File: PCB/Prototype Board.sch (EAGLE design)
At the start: 65 parts, among them J1 USB Type C, J3 Connector, J4 Battery Connector, Q1 S8050, Q10 20V/0.2A/8MHz/1.2Ω/1Vth, Q12 20V/0.2A/8MHz/1.2Ω/1Vth, Q14 20V/0.2A/8MHz/1.2Ω/1Vth, Q16 20V/0.2A/8MHz/1.2Ω/1Vth, Q3 20V/4.2A/52mΩ/1.4W, Q4 S8050, Q6 20V/0.2A/8MHz/1.2Ω/1Vth, Q8 20V/0.2A/8MHz/1.2Ω/1Vth, U1 9DoF IMU, U2 MCP73831, U3 ESP-WROOM-32, U5 DWM1000, U6 1.8V/100mA, U7 CH340C, U8 XC6222B331MR-G

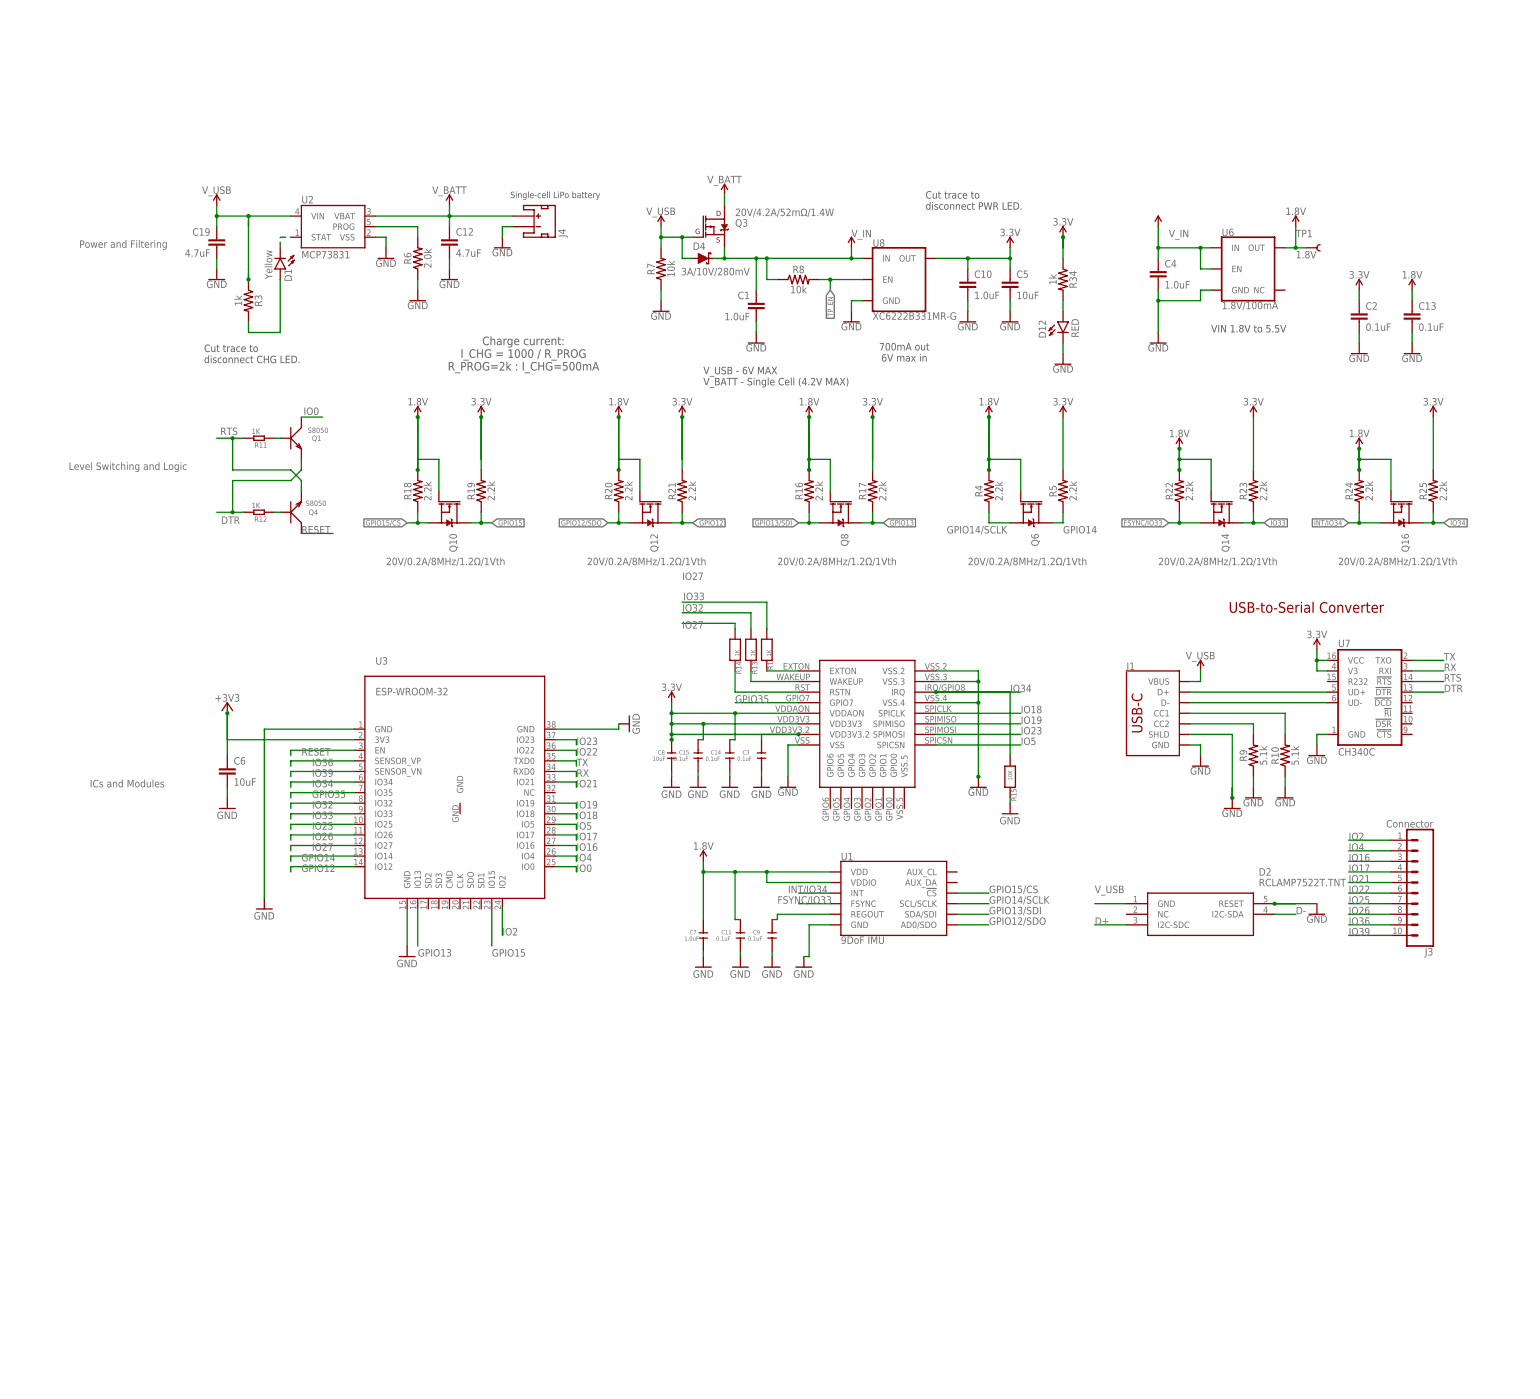
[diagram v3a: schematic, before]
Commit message: Grouped Schematic
Components selected, laid out, not routed yet
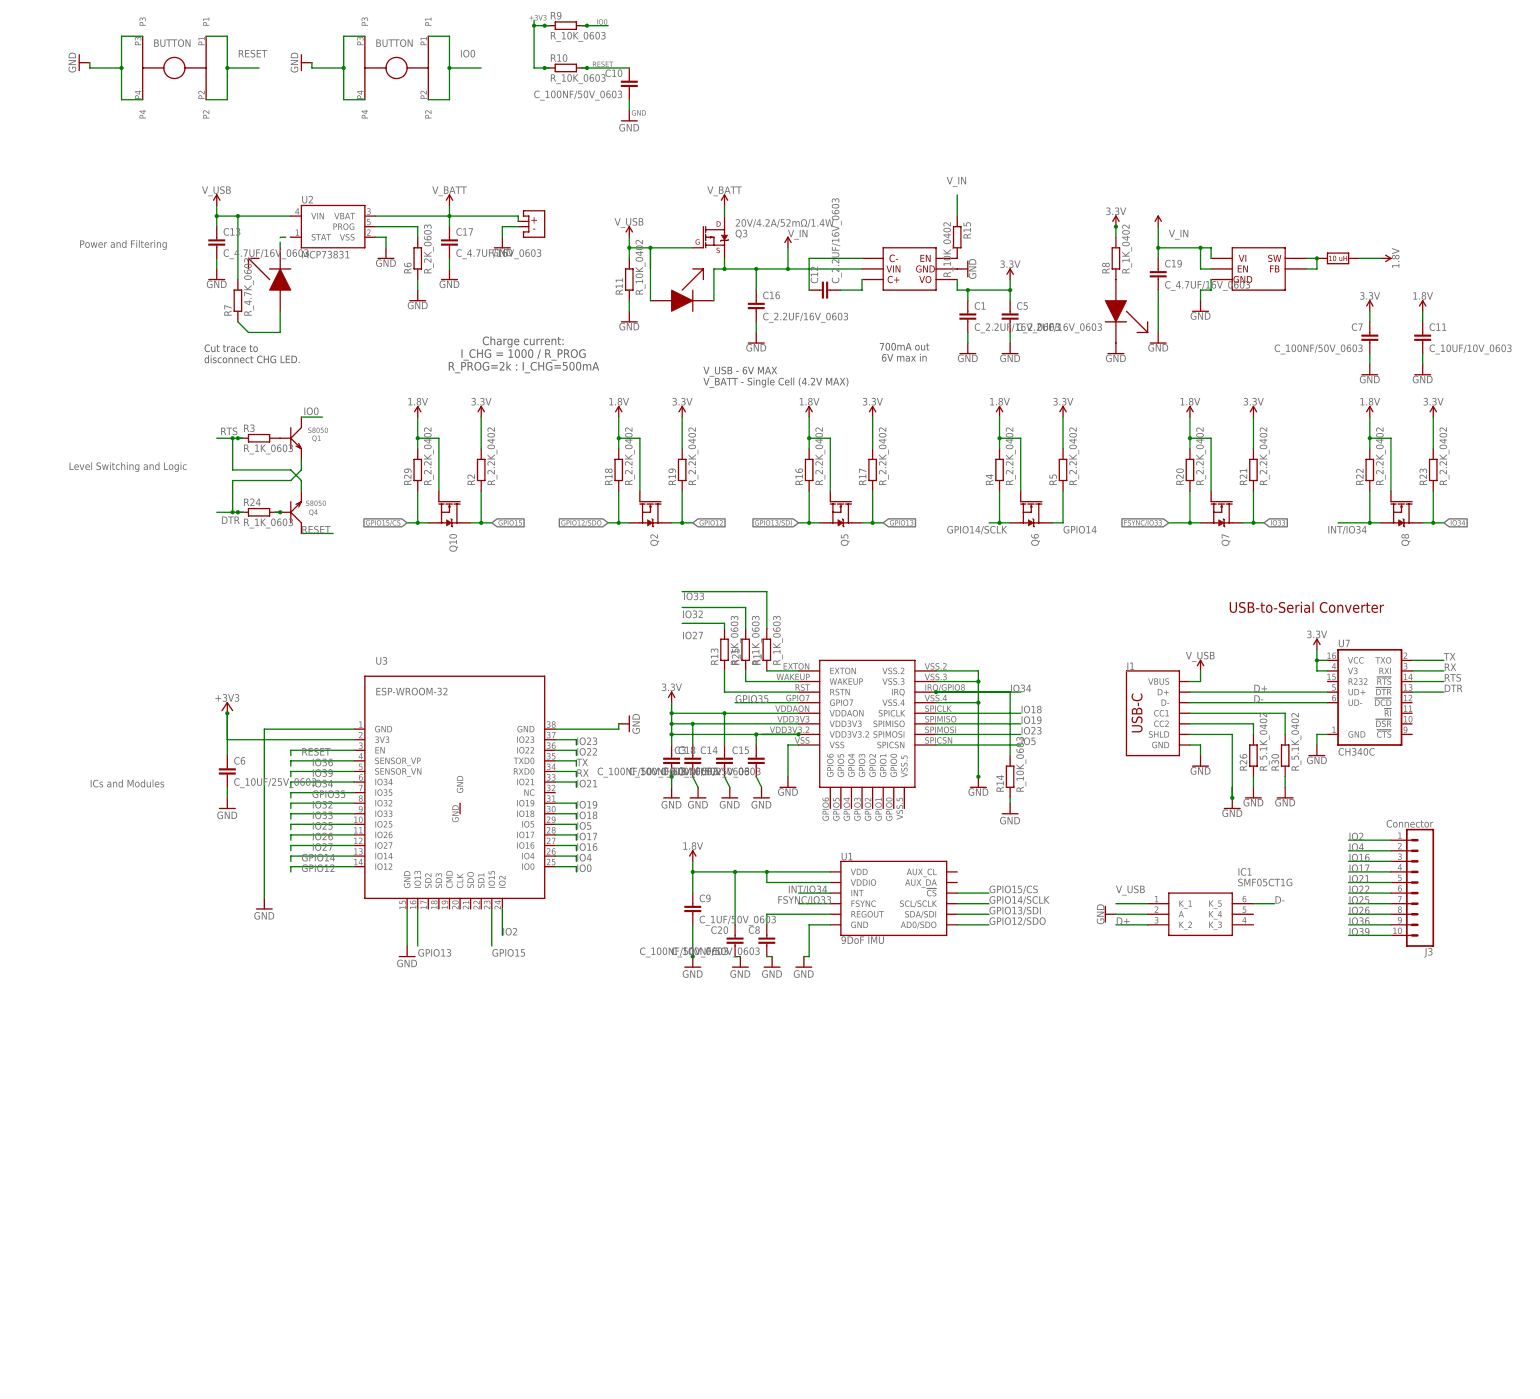
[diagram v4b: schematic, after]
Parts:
- removed C2: 0.1uF, SparkFun-Capacitors:0.1UF-0402-16V-10%
- removed C4: 1.0uF, SparkFun-Capacitors:1.0UF-0402-16V-10%
- removed D1: Yellow, SparkFun-LED:LED-YELLOW0603
- removed D12: RED, SparkFun-LED:LED-RED0603
- removed D2: RCLAMP7522T.TNT, RCLAMP7522T.TNT:RCLAMP7522T.TNT
- removed D4: 3A/10V/280mV, SparkFun-DiscreteSemi:DIODE-SCHOTTKY-BAT60A
- removed J4: Battery Connector, SparkFun-Connectors:JST_2MM_MALE
- removed Q16: 20V/0.2A/8MHz/1.2Ω/1Vth, SparkFun-DiscreteSemi:MOSFET-NCH-RE1C002UN
- removed R12: 1K, Discrete:R-0603
- removed R34: 1k, SparkFun-Resistors:1KOHM-0402T-1/16W-1%
- removed TP1: 1.8V, SparkFun-Connectors:TEST-POINT3
- removed U6: 1.8V/100mA, SparkFun-IC-Power:V_REG_SP6214-1.8V
- removed U8: XC6222B331MR-G, SparkFun-IC-Power:XC6222B331MR-G
- added C16: C_2.2UF/16V_0603, JLC PCB Basic Parts_loc:C_2.2UF/16V_0603
- added C17: C_4.7UF/16V_0603, JLC PCB Basic Parts_loc:C_4.7UF/16V_0603
- added C18: C_10UF/25V_0603, JLC PCB Basic Parts_loc:C_10UF/25V_0603
- added C20: C_100NF/50V_0603, JLC PCB Basic Parts_loc:C_100NF/50V_0603
- added IC1: SMF05CT1G, SMF05CT1G:SMF05CT1G
- added Q5: 20V/0.2A/8MHz/1.2Ω/1Vth, SparkFun-DiscreteSemi:MOSFET-NCH-RE1C002UN
- added R2, R29: R_2.2K_0402, JLC PCB Basic Parts_loc:R_2.2K_0402
- added R26, R30: R_5.1K_0402, JLC PCB Basic Parts_loc:R_5.1K_0402
- added U$1, U$3: K2-6639SP-C4SC-04_C83206, customlib:K2-6639SP-C4SC-04_C83206
- added U$2: MLF2012, customlib:MLF2012
- added U$4: TPS62202DBVR, customlib:TPS62202DBVR
- added U$5: HE9008M6R, customlib:HE9008M6R
- added U$6, U$7, U$9: 19-217/GHC-YR1S2/3T, customlib:19-217/GHC-YR1S2/3T
- added U$8: SM02B_PASS_TB_LF, customlib:SM02B_PASS_TB_LF
- C1: value 1.0uF -> C_2.2UF/16V_0603; device SparkFun-Capacitors:1.0UF-0402-16V-10% -> JLC PCB Basic Parts_loc:C_2.2UF/16V_0603
- C10: value 1.0uF -> C_100NF/50V_0603; device SparkFun-Capacitors:1.0UF-0402-16V-10% -> JLC PCB Basic Parts_loc:C_100NF/50V_0603
- C11: value 0.1uF -> C_10UF/10V_0603; device Discrete:C-0603 -> JLC PCB Basic Parts_loc:C_10UF/10V_0603
- C12: value 4.7uF -> C_2.2UF/16V_0603; device SparkFun-Capacitors:4.7UF-1206-16V-(+80/-20%) -> JLC PCB Basic Parts_loc:C_2.2UF/16V_0603
- C13: value 0.1uF -> C_4.7UF/16V_0603; device SparkFun-Capacitors:0.1UF-0402-16V-10% -> JLC PCB Basic Parts_loc:C_4.7UF/16V_0603
- C14, C15, C3: value 0.1uF -> C_100NF/50V_0603; device Discrete:C-0603 -> JLC PCB Basic Parts_loc:C_100NF/50V_0603
- C19: value 4.7uF -> C_4.7UF/16V_0603; device SparkFun-Capacitors:4.7UF-1206-16V-(+80/-20%) -> JLC PCB Basic Parts_loc:C_4.7UF/16V_0603
- C5: value 10uF -> C_2.2UF/16V_0603; device SparkFun-Capacitors:10UF-0603-6.3V-20% -> JLC PCB Basic Parts_loc:C_2.2UF/16V_0603
- C6: value 10uF -> C_10UF/25V_0603; device rcl:C-EUC0603 -> JLC PCB Basic Parts_loc:C_10UF/25V_0603
- C7: value 1.0uF -> C_100NF/50V_0603; device Discrete:C-0603 -> JLC PCB Basic Parts_loc:C_100NF/50V_0603
- C8: value 10uF -> C_100NF/50V_0603; device Discrete:C-0603 -> JLC PCB Basic Parts_loc:C_100NF/50V_0603
- C9: value 0.1uF -> C_1UF/50V_0603; device Discrete:C-0603 -> JLC PCB Basic Parts_loc:C_1UF/50V_0603
- R1, R13: value 1K -> R_1K_0603; device microbuilder:RESISTOR_0603_NOOUT -> JLC PCB Basic Parts_loc:R_1K_0603
- R10, R9: value 5.1k -> R_10K_0603; device SparkFun-Resistors:5.1KOHM-0402T-1/16W-1% -> JLC PCB Basic Parts_loc:R_10K_0603
- R11: value 1K -> R_10K_0402; device Discrete:R-0603 -> JLC PCB Basic Parts_loc:R_10K_0402
- R14: value 1K -> R_10K_0603; device microbuilder:RESISTOR_0603_NOOUT -> JLC PCB Basic Parts_loc:R_10K_0603
- R15: value 10K -> R_10K_0402; device microbuilder:RESISTOR_0603_NOOUT -> JLC PCB Basic Parts_loc:R_10K_0402
- R16, R17, R18, R19, R20, R21, R22, R23, R4, R5: value 2.2k -> R_2.2K_0402; device SparkFun-Resistors:2.2KOHM-0402T-1/16W-1% -> JLC PCB Basic Parts_loc:R_2.2K_0402
- R24, R25: value 2.2k -> R_1K_0603; device SparkFun-Resistors:2.2KOHM-0402T-1/16W-1% -> JLC PCB Basic Parts_loc:R_1K_0603
- R3: value 1k -> R_1K_0603; device SparkFun-Resistors:1KOHM-0402T-1/16W-1% -> JLC PCB Basic Parts_loc:R_1K_0603
- R6: value 2.0k -> R_2K_0603; device SparkFun-Resistors:2.0KOHM-0603-1/10W-5% -> JLC PCB Basic Parts_loc:R_2K_0603
- R7: value 10k -> R_4.7K_0603; device SparkFun-Resistors:10KOHM-0402T-1/16W-1% -> JLC PCB Basic Parts_loc:R_4.7K_0603
- R8: value 10k -> R_1K_0402; device SparkFun-Resistors:10KOHM-0402T-1/16W-1% -> JLC PCB Basic Parts_loc:R_1K_0402
- renumbered Q12 to Q2, Q14 to Q7
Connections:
- removed net N$30: D12.A, R34.2
- removed net TP_EN: R8.2, U8.EN
- new net N$15: C12.2, U$5.C+
- new net N$4: R8.1, U$9.1
- new net N$8: U$2.P$1, U$4.FB, U$4.SW
- new net N$9: R15.2, U$5.EN
- net +3V3: now also R10.1, R9.1
- net 1.8V: now also C20.1, C9.1, Q2.G, Q5.G, R20.2, R29.2, U$2.P$2; no longer C13.1, C7.1, Q16.G, R24.2, TP1.1, U6.OUT
- net 3.3V: now also C1.1, C18.1, C7.1, R2.2, R8.2, U$5.VO; no longer C10.1, C2.1, C8.1, R25.2, R34.1, U8.OUT
- net CHG_LED: now also R7.1, U$6.1; no longer D1.A, R3.2
- net D+: now also IC1.K_2; no longer D2.I2C-SDC
- net D-: now also IC1.K_5; no longer D2.I2C-SDA
- net DTR: now also R24.1; no longer R12.2
- net FSYNC/IO33: now also R20.1; no longer R22.1
- net GND: now also C16.2, C17.2, C18.2, C20.2, IC1.A, R11.1, R14.1, R26.1, R30.1, U$1.P3, U$1.P4, U$3.P3, U$3.P4, U$4.GND, U$5.GND, U$8.-, U$9.2; no longer C12.2, C2.2, C4.2, D12.C, D2.RESET, J4.-, R10.1, R15.2, R7.1, R9.1, U6.GND, U8.GND
- net GPIO12: now also R19.1; no longer R21.1
- net GPIO12/SDO: now also R18.1; no longer R20.1
- net GPIO13: now also Q5.D; no longer Q8.D
- net GPIO13/SDI: now also Q5.S; no longer Q8.S
- net GPIO15: now also R2.1; no longer R19.1
- net GPIO15/CS: now also R29.1; no longer R18.1
- net INT/IO34: now also Q8.S, R22.1; no longer Q16.S, R24.1
- net IO0: now also R9.2, U$3.P1, U$3.P2
- net IO27: now also R13.2; no longer R14.1
- net IO32: now also R25.2; no longer R13.1
- net IO33: now also R1.2, R21.1; no longer R1.1, R23.1
- net IO34: now also Q8.D, R14.2, R23.1; no longer Q16.D, R15.1, R25.1
- net N$1: now also R24.2; no longer R12.1
- net N$10: now also R1.1; no longer R1.2
- net N$11: now also R25.1; no longer R13.2
- net N$12: now also R13.1; no longer R14.2
- net N$13: now also C8.1; no longer C9.1
- net N$14: now also C12.1, U$5.C-; no longer Q1.B, R11.1
- net N$2: now also Q1.B, R3.2; no longer Q2.G, R20.2
- net N$5: now also R26.2; no longer R9.2
- net N$6: now also R30.2; no longer R10.2
- net N$7: now also U$6.2; no longer D1.C
- net RESET: now also C10.1, R10.2, U$1.P1, U$1.P2
- net RTS: now also R3.1; no longer R11.2
- net V_BATT: now also C17.1, U$8.+; no longer C12.1, J4.+
- net V_IN: now also C16.1, C19.1, R15.1, U$4.EN, U$4.VI, U$5.VIN, U$7.2; no longer C1.1, C4.1, D4.C, R8.1, U6.EN, U6.IN, U8.IN
- net V_USB: now also C13.1, IC1.K_1, R11.2, U$7.1; no longer C19.1, D2.GND, D4.A, R3.1
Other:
- note removed: "Cut trace to disconnect PWR LED."
- note removed: "Single-cell LiPo battery"
- note removed: "VIN 1.8V to 5.5V"
- moved on the sheet: Q3, Q8

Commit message: Board Almost Finished
Need to route IO connectors, retouch design rules, clean up connections, etc
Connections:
- net D+ renamed D_P
- net D- renamed D_N
- net FSYNC/IO33 renamed FSYNC/IO36
- net INT/IO34 renamed INT/IO39
- net RX renamed RX-TX_P
- net TX renamed RX-TX_N
- removed net +3V3: C6.1, R10.1, R9.1, U3.3V3
- net 3.3V: now also C6.1, R10.1, R9.1, U3.3V3
- net GND: now also U5.VSS.5
- net IO16: no longer J3.3
- net IO17: no longer J3.4
- net IO2: no longer J3.1
- net IO21: no longer J3.5
- net IO22: no longer J3.6
- net IO25: no longer J3.7
- net IO26: no longer J3.8
- net IO33: no longer Q7.D, R21.1
- net IO34: no longer Q8.D, R23.1
- net IO36: now also Q7.D, R21.1; no longer J3.9
- net IO39: now also Q8.D, R23.1; no longer J3.10
- net IO4: no longer J3.2
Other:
- moved on the sheet: C14, C15, C18, C3, C7, R1, R13, R14, R25

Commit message: Resolved half of the warnings
Will need to look into the USB footprint. Looks odd
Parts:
- added J2, J4, J5, J6, J7, J8, J9: (no value), SparkFun-Connectors:CONN_01PTH_2MM
- J3: value Connector -> (none); device SparkFun-Connectors:CONN_10" -> SparkFun-Connectors:CONN_01PTH_2MM
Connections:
- new net DW3: J4.1, U5.GPIO3
- new net DW4: J5.1, U5.GPIO4
- new net DW5: J6.1, U5.GPIO5
- new net DW6: J7.1, U5.GPIO6
- net IO21: now also J3.1
- net IO22: now also J2.1
- net IO25: now also J8.1
- net IO26: now also J9.1
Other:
- moved on the sheet: C14, C15, C18, C3, R1, R13, R14, R25

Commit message: Resolved all DRC violations
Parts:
- removed J1: USB Type C, SparkFun-Connectors:USB_C_2-LAYER_PADS
- removed R26, R30: R_5.1K_0402, JLC PCB Basic Parts_loc:R_5.1K_0402
- added R12, R27: R_5.1K_0402, JLC PCB Basic Parts_loc:R_5.1K_0402
- added U$10: USBC19, customlib:USBC19
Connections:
- removed net N$5: J1.CC2, R26.2
- removed net N$6: J1.CC1, R30.2
- new net N$16: R27.2, U$10.B5
- new net N$17: R12.2, U$10.A5
- net D_N: now also U$10.A7, U$10.B7; no longer J1.D-
- net D_P: now also U$10.A6, U$10.B6; no longer J1.D+
- net GND: now also R12.1, R27.1, U$10.A12; no longer J1.GND, J1.SHLD, R26.1, R30.1
- net V_USB: now also U$10.A4; no longer J1.VBUS

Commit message: Completed First Draft of PCB + Assembly Details
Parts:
- removed C18: C_10UF/25V_0603, JLC PCB Basic Parts_loc:C_10UF/25V_0603
- removed C20: C_100NF/50V_0603, JLC PCB Basic Parts_loc:C_100NF/50V_0603
- removed IC1: SMF05CT1G, SMF05CT1G:SMF05CT1G
- removed U7: CH340C, SparkFun-IC-Comms:CH340C
- added C2, C4: C_10UF/10V_0603, JLC PCB Basic Parts_loc:C_10UF/10V_0603
- added D1: BAT60AE6327HTSA1, BAT60AE6327HTSA1:BAT60AE6327HTSA1
- added U$11: CH340B, customlib:CH340B
- C6: value C_10UF/25V_0603 -> 1.0uF; device JLC PCB Basic Parts_loc:C_10UF/25V_0603 -> SparkFun-Capacitors:1.0UF-0603-16V-10%-X7R
- C8: value C_100NF/50V_0603 -> 0.1uF; device JLC PCB Basic Parts_loc:C_100NF/50V_0603 -> SparkFun-Capacitors:0.1UF-0603-25V-5%
- C9: value C_1UF/50V_0603 -> 0.1uF; device JLC PCB Basic Parts_loc:C_1UF/50V_0603 -> SparkFun-Capacitors:0.1UF-0603-25V-5%
- U$7: value 19-217/GHC-YR1S2/3T -> TPSMF05CT1G; device customlib:19-217/GHC-YR1S2/3T -> customlib:TPSMF05CT1G
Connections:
- net 1.8V: now also C6.1, C8.1; no longer C20.1, C9.1
- net 3.3V: now also C2.1, C4.1, U$11.V3, U$11.VCC; no longer C18.1, C6.1, U7.V3, U7.VCC
- net DTR: now also U$11.DTR; no longer U7.!DTR
- net D_N: now also U$11.UD-, U$7.6; no longer IC1.K_5, U7.UD-
- net D_P: now also U$11.UD+, U$7.3; no longer IC1.K_2, U7.UD+
- net GND: now also C2.2, C4.2, U$11.GND, U$7.2; no longer C18.2, C20.2, IC1.A, U7.GND
- net N$13: now also C9.1; no longer C8.1
- net RTS: now also U$11.RTS; no longer U7.!RTS
- net RX-TX_N: now also U$11.TXD; no longer U7.TXO
- net RX-TX_P: now also U$11.RXD; no longer U7.RXI
- net V_IN: now also D1.K; no longer U$7.2
- net V_USB: now also D1.A; no longer IC1.K_1
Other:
- moved on the sheet: C3
